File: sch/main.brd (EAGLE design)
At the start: 50.5 x 49.5 mm, 37 parts

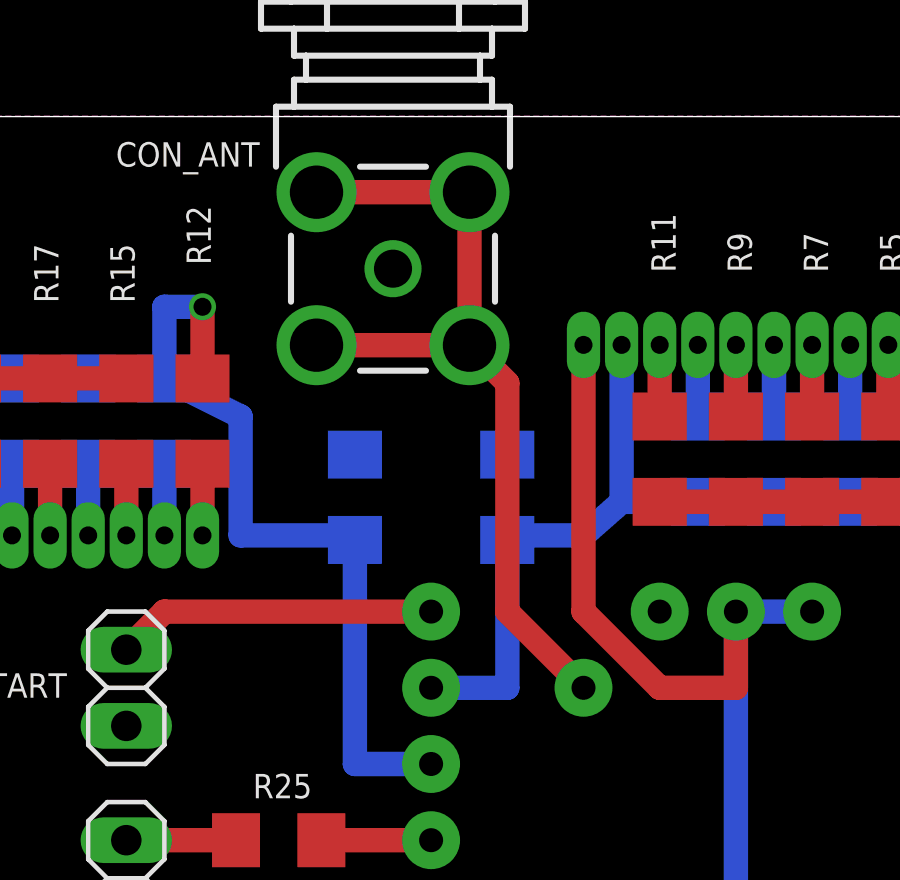
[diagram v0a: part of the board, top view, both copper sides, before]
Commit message: [ fix ] gnd ant signal inversion
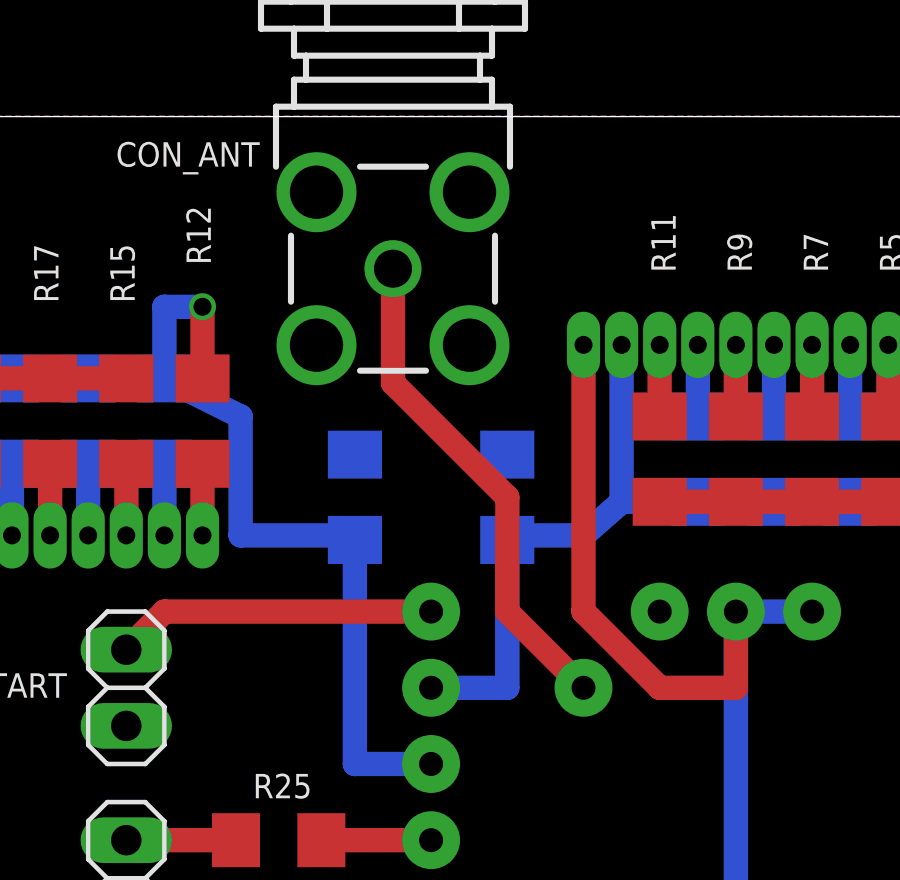
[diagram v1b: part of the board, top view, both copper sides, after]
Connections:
- net ANT: now also CON_ANT.1; no longer CON_ANT.2, CON_ANT.3, CON_ANT.4, CON_ANT.5
- net GND: now also CON_ANT.2, CON_ANT.3, CON_ANT.4, CON_ANT.5; no longer CON_ANT.1
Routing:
- net ANT: track 28.3 -> 16.6 mm
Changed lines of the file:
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@@
 <vertex x="0" y="0"/>
 </polygon>
-<contactref element="CON_ANT" pad="1"/>
 <wire x1="42.14" y1="11.43" x2="41.91" y2="11.43" width="0.8128" layer="16"/>
 <wire x1="41.91" y1="11.43" x2="41.91" y2="7.62" width="0.8128" layer="16"/>
 <wire x1="41.91" y1="7.62" x2="39.37" y2="5.08" width="0.8128" layer="16"/>
 <wire x1="39.37" y1="5.08" x2="33.25" y2="5.08" width="0.8128" layer="16"/>
+<contactref element="CON_ANT" pad="2"/>
+<contactref element="CON_ANT" pad="4"/>
+<contactref element="CON_ANT" pad="5"/>
+<contactref element="CON_ANT" pad="3"/>
 </signal>
 <signal name="VREG_33">
@@
 <signal name="ANT">
 <contactref element="U$1" pad="ANT"/>
-<wire x1="29.21" y1="40.64" x2="29.21" y2="33.02" width="0.8128" layer="1"/>
-<wire x1="29.21" y1="33.02" x2="31.75" y2="30.48" width="0.8128" layer="1"/>
-<contactref element="CON_ANT" pad="2"/>
-<contactref element="CON_ANT" pad="4"/>
-<contactref element="CON_ANT" pad="5"/>
-<contactref element="CON_ANT" pad="3"/>
-<wire x1="29.21" y1="40.64" x2="27.9499" y2="41.91" width="0.8128" layer="1"/>
-<wire x1="27.9499" y1="41.91" x2="27.9499" y2="41.9001" width="0.8128" layer="1"/>
-<wire x1="27.9499" y1="41.91" x2="27.9499" y2="46.9999" width="0.8128" layer="1"/>
-<wire x1="27.9499" y1="46.9999" x2="22.8501" y2="46.9999" width="0.8128" layer="1"/>
-<wire x1="27.9499" y1="41.9001" x2="22.8501" y2="41.9001" width="0.8128" layer="1"/>
+<contactref element="CON_ANT" pad="1"/>
+<wire x1="31.75" y1="30.48" x2="29.21" y2="33.02" width="0.8128" layer="1"/>
+<wire x1="29.21" y1="33.02" x2="29.21" y2="36.83" width="0.8128" layer="1"/>
+<wire x1="29.21" y1="36.83" x2="25.4" y2="40.64" width="0.8128" layer="1"/>
+<wire x1="25.4" y1="40.64" x2="25.4" y2="44.45" width="0.8128" layer="1"/>
 </signal>
 <signal name="BUT_START">

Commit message: [ update ] schematics version, silkscreen
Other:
- board text added: "17e22f8ac59524"
- board text added: "ooklone_v0001"
- board text removed: "c7f8af5fd91c20"
- board text removed: "ooklone_v0000"
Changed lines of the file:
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@@
 <hole x="2.54" y="46.99" drill="2.8"/>
 <hole x="2.54" y="2.54" drill="2.8"/>
-<text x="6.35" y="17.78" size="0.8128" layer="25">ooklone_v0000</text>
-<text x="6.35" y="16.51" size="0.8128" layer="25">c7f8af5fd91c20</text>
+<text x="6.35" y="17.78" size="0.8128" layer="25">ooklone_v0001</text>
+<text x="6.35" y="16.51" size="0.8128" layer="25">17e22f8ac59524</text>
 </plain>
 <attributes>
